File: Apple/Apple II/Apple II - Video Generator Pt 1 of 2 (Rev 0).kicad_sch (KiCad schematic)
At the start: 0 parts

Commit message: Finished Apple II - Sheet 14 - Video Generator Part 1 (Rev 0)
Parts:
- added A10: 74LS194, symbol Apple II:A10_74LS194
- added A3: 74166, symbol Apple II:A3_74166
- added A9: 74LS151, symbol Apple II:A9_74LS151
- added B10: 74LS74, symbol Apple II:B10_74LS74
- added B11: 74LS08, symbol Apple II:B11_74LS08
- added B12: 74LS11, symbol Apple II:B12_74LS11
- added B13: 74LS02, symbol Apple II:B13_74LS02
- added B2: 74S86, symbol Apple II:B2_74S86
- added B4: 74LS194, symbol Apple II:B4_74LS194
- added B9: 74LS194, symbol Apple II:B9_74LS194
- added C15: 0.1µF, symbol Device:C_Small
- added R12: 12K, symbol Device:R_US
- added R13: 3.3M, symbol Device:R_US
- added U?: A8_74LS257, symbol Apple II:A8_74LS257
- added U? (x2): B8_74LS174, symbol Apple II:B8_74LS174
- added U?: B5_74LS174, symbol Apple II:B5_74LS174
- added U?: B3_555, Package_SO:SOIC-8_3.9x4.9mm_P1.27mm, symbol Apple II:B3_555
- added U?: A5_2513, symbol Apple II:A5_2513
- added U?: B11_74LS08, symbol Apple II:B11_74LS08
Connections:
- new net: A10.4 (D1), U?.12 (ZD)
- new net: A9.15 (D4), B4.15 (Q0), U?.2 (0A)
- new net: A9.13 (D6), B9.15 (Q0), B9.7 (DSL), U?.3 (1A)
- new net: B4.7 (DSL), U?.4 (ZA)
- new net: A10.3 (D0), U?.7 (ZB)
- new net: B4.10 (S1), U?.9 (ZC)
- new net: A10.6 (D3), A3.2 (A), B13.4
- new net: B11.11, B13.5
- new net: A9.9 (C), U?.2 (Q0), U?.5
- new net: U?.15 (Q5), U?.3 (D0)
- new net: U?.14 (D4), U?.2 (Q0)
- new net: B13.13, U?.3 (D0)
- new net: R12.1, R13.2, U?.7 (DIS)
- new net: A10.12 (Q3), A3.1 (SER.IN), B2.12
- new net: A10.13 (Q2), A9.7 (~{ST})
- new net: A10.14 (Q1), A9.11 (A)
- new net: A10.15 (Q0), A9.10 (B)
- new net: B4.10 (S1), B9.10 (S1)
- new net: B4.11, B9.11
- new net: A9.14 (D5), B4.13 (Q2)
- new net: B4.9 (S0), B9.9 (S0)
- new net: A9.12 (D7), B9.13 (Q2)
- new net: C15.2, R13.1, U?.2 (TR), U?.6 (TH)
- new net: B11.13, U?.3 (OUT)
- new net: A9.1 (D3), A9.2 (D2), A9.3 (D1), A9.4 (D0), B2.11
- new net: A3.13 (Q_{H}), B2.13
- new net: A3.4 (C), U?.4 (D1)
- new net: A3.5 (D), U?.5 (D2)
- new net: A3.10 (E), U?.6 (D3)
- new net: A3.11 (F), U?.7 (D4)
- new net: A3.12 (G), U?.8 (D5)
- new net: B12.6, B13.11
- new net +5V: R12.2, U?.4 (~{R}), U?.8 (VCC)
- new net 14M: A10.11 (Cp), A3.7 (CL2), A9.5 (Y), B10.2 (D), B10.3 (CLK), B4.11, U?.1 (S), U?.4
- new net 7M_{36}: A3.6 (CL1)
- new net BLANKING: A10.5 (D2)
- new net DL0: B4.3 (D0), U?.17 (A4)
- new net DL1: B4.4 (D1), U?.18 (A5)
- new net DL2: B4.5 (D2), U?.19 (A6)
- new net DL3: B4.6 (D3), U?.20 (A7)
- new net DL4: B9.3 (D0), U?.21 (A8)
- new net DL5: B9.4 (D1), U?.22 (A9)
- new net DL6: B11.12, B9.5 (D2)
- new net DL7: B13.6, B9.6 (D3)
- new net Earth: A3.14 (H), A3.3 (B), C15.1, U?.1 (GND), U?.10 (GND), U?.11 (~{CE}), U?.13 (1D), U?.15 (~{E}), U?.6 (1B)
- new net H0: U?.14 (0D)
- new net HIRES: U?.6
- new net LD194: A10.10 (S1), A10.9 (S0), B4.9 (S0)
- new net MIX MODE: B12.5
- new net SOFT 5: A3.9 (~{CLR}), B10.1 (~{CLR}), B10.4 (~{P}), U?.1 (~{CLR}), U?.1 (~{CLR}), U?.1 (~{CLR}), U?.11 (0C)
- new net TEXT MODE: B13.12
- new net V2: B12.3
- new net V4: B12.4
- new net VA: U?.14 (A1)
- new net VB: U?.15 (A2)
- new net VC: U?.16 (A3), U?.5 (0B)
- new net VIDEO_DATA: B10.5 (Q)
- new net ~{7M}: U?.10 (1C)
- new net ~{LDPS}: A3.15 (~{LD})
- new net ~{RAS}: U?.9 (Cp), U?.9 (Cp), U?.9 (Cp)
- no-connect marks 0 -> 1
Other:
- note added: "FROM CLOCK GENERATOR"
- note added: "FROM ON-BOARD I/O"
- note added: "FROM PART 2"
- note added: "FROM RAM"
- note added: "FROM VIDEO ADDRESS GENERATOR"
- note added: "TO MEMORY ADDRESS"
- note added: "TO PART 2"
- title: (none) -> Apple II - Video Generator Part 1

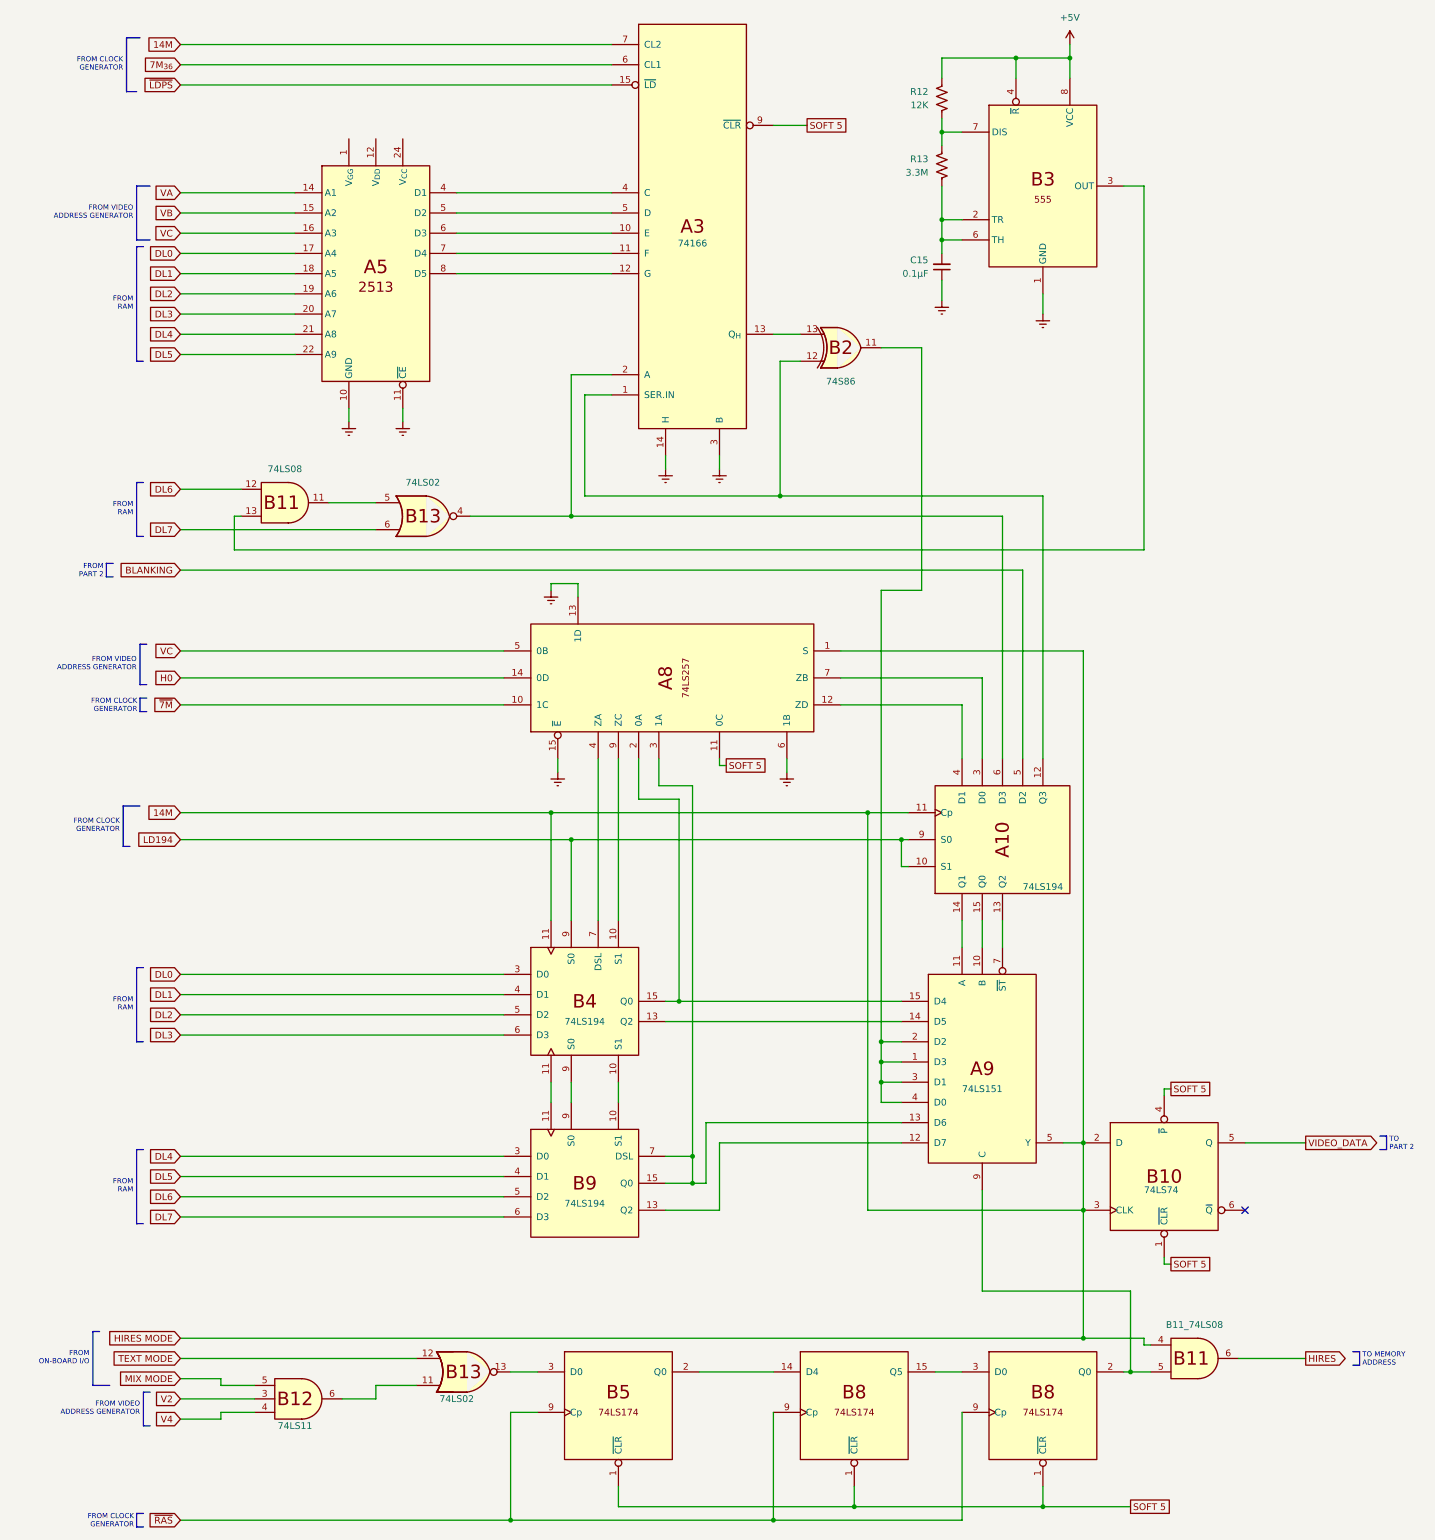
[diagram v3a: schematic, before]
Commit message: Finished Apple II - Sheet 15 - Video Generator Part 1 (Rev 1)
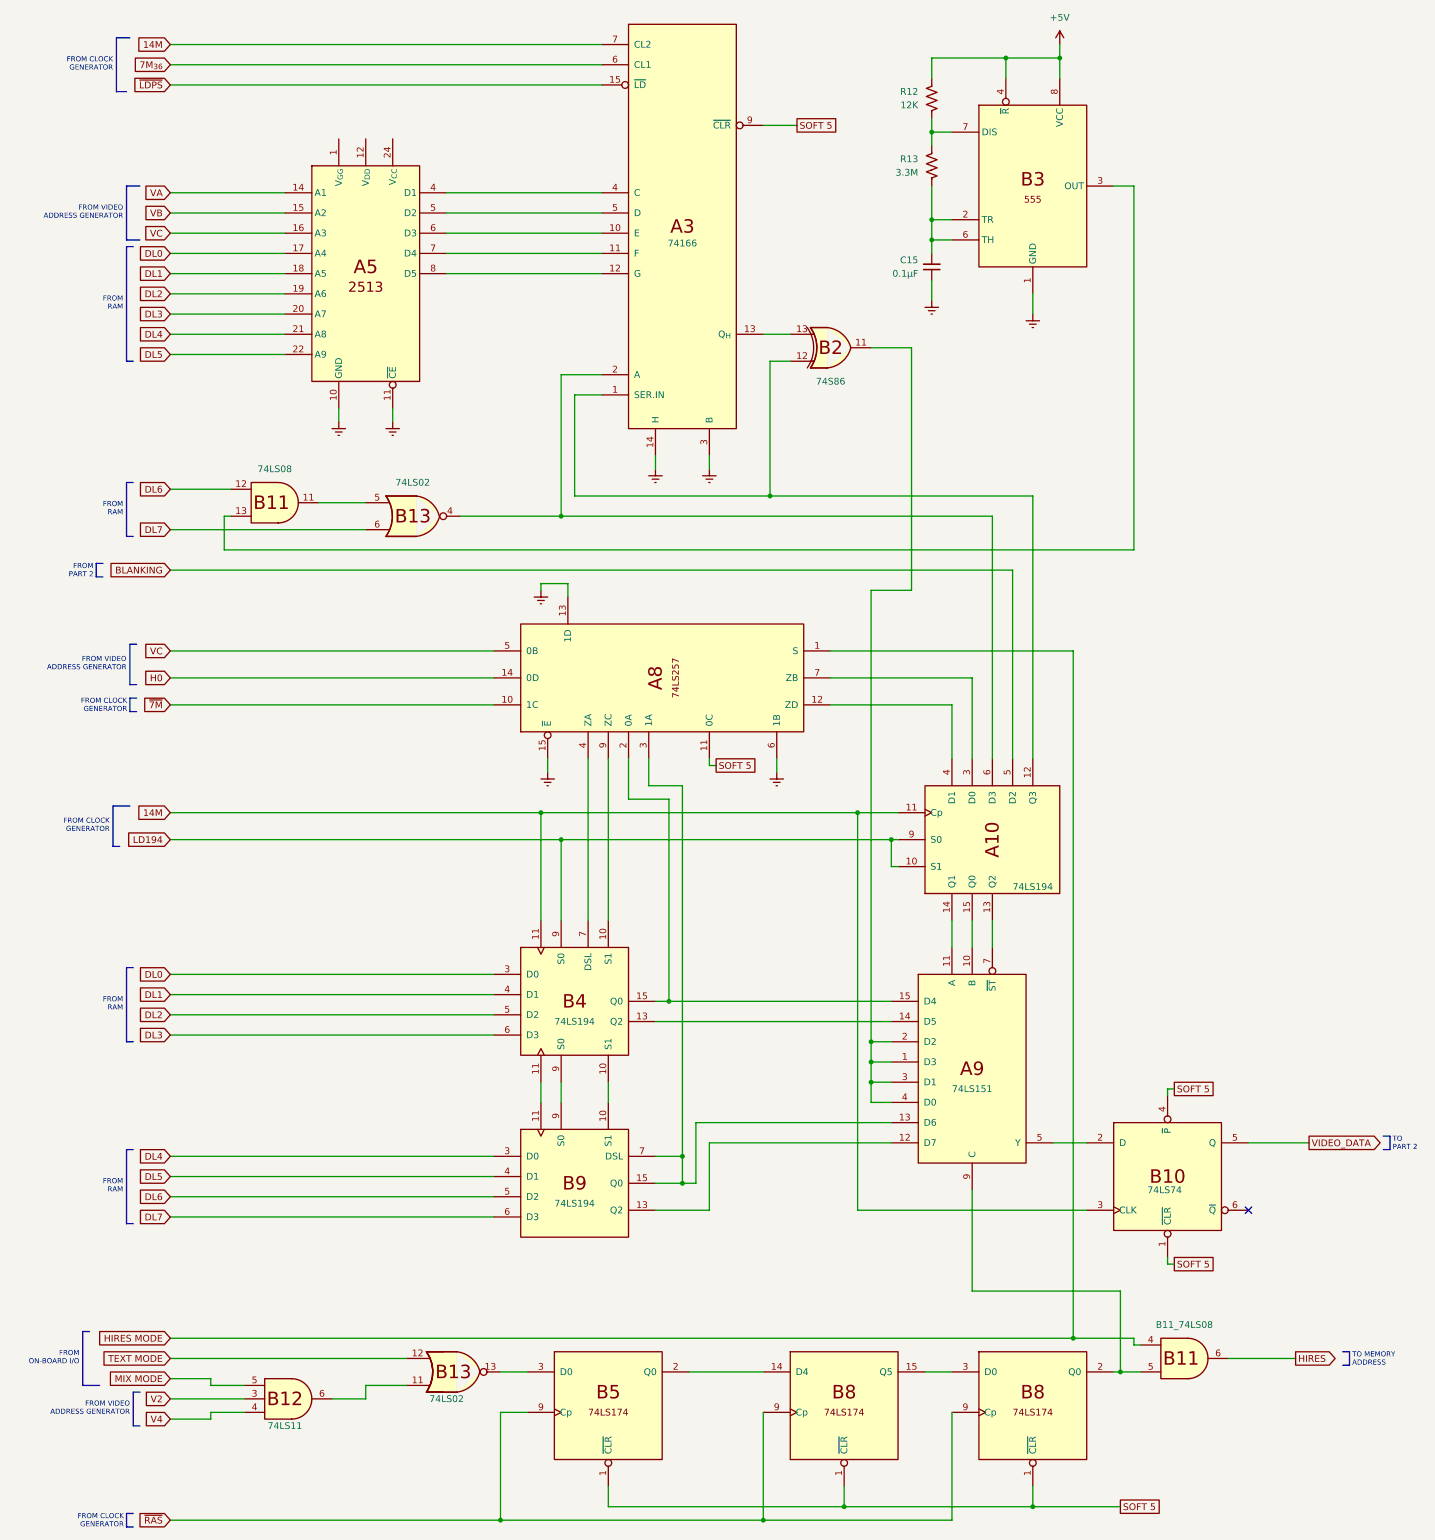
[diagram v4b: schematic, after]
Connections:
- net 14M: no longer A9.5 (Y), B10.2 (D), U?.1 (S), U?.4
- new net: A9.5 (Y), B10.2 (D)
- new net HIRES MODE: U?.1 (S), U?.4
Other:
- moved on the sheet: C15, R12, R13

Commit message: Finished Apple II - Sheet 16 - Video Generator Part 1 (Rev 7, RFI)
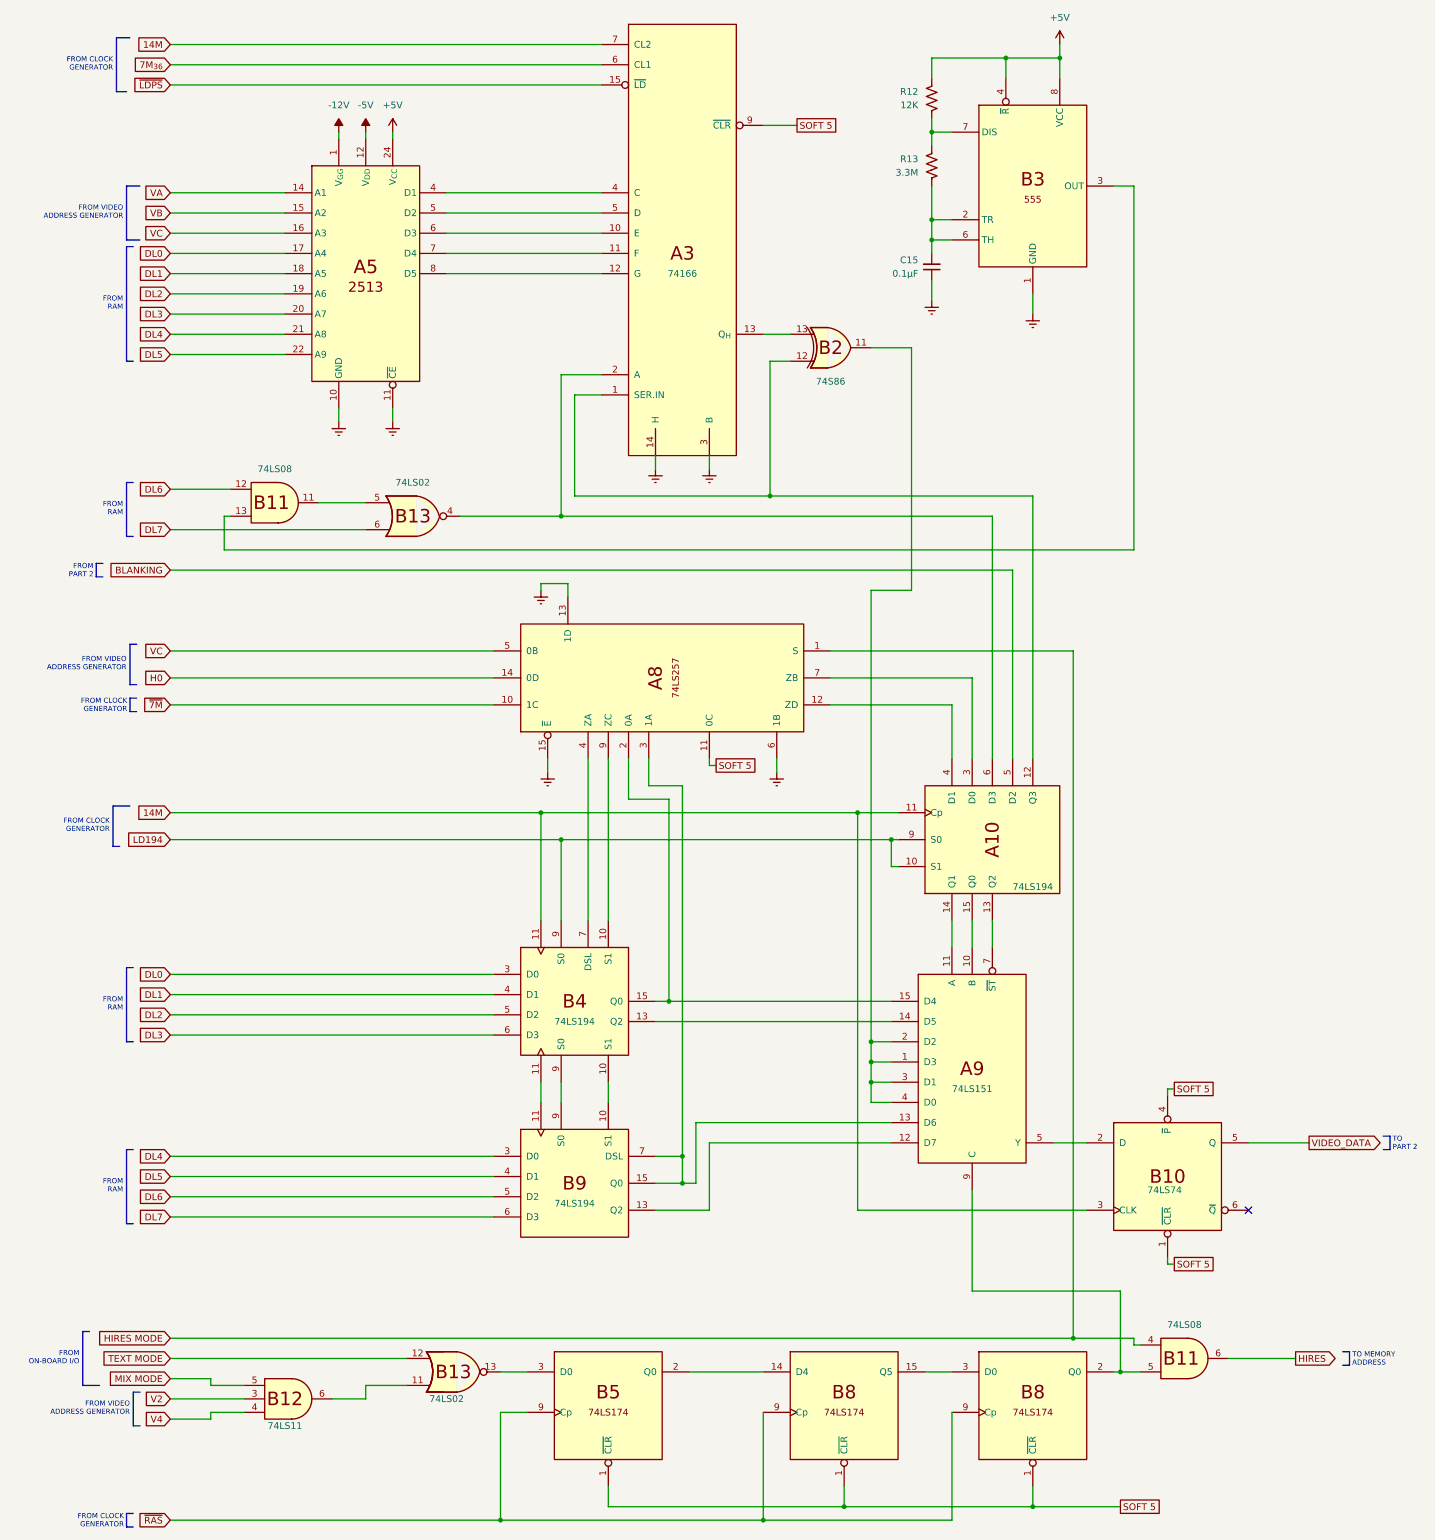
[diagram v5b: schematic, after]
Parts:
- B11: renamed from U?; value B11_74LS08 -> 74LS08
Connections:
- net +5V: now also U?.24 (V_{CC})
- net -12V: now reaches U?.1 (V_{GG})
- net -5V: now reaches U?.12 (V_{DD})
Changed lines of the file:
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@@
+    (stroke (width 0) (type default) (color 0 0 0 0))
+  )
+  (wire (pts (xy 82.55 76.2) (xy 82.55 77.47))
     (stroke (width 0) (type default) (color 0 0 0 0))
   )
@@
     (stroke (width 0) (type default) (color 0 0 0 0))
   )
+  (wire (pts (xy 87.63 76.2) (xy 87.63 77.47))
+    (stroke (width 0) (type default) (color 0 0 0 0))
+  )
   (polyline (pts (xy 38.735 281.94) (xy 37.465 281.94))
     (stroke (width 0) (type solid) (color 0 0 0 0))
@@
   )
   (wire (pts (xy 162.56 114.3) (xy 157.48 114.3))
+    (stroke (width 0) (type default) (color 0 0 0 0))
+  )
+  (wire (pts (xy 77.47 76.2) (xy 77.47 77.47))
     (stroke (width 0) (type default) (color 0 0 0 0))
   )
@@
     )
     (property "Datasheet" "~" (id 3) (at 147.32 139.7 0)
+      (effects (font (size 1.27 1.27)) hide)
+    )
+    (pin "1")
+  )
+  (symbol (lib_id "power:-12V") (at 77.47 76.2 0) (unit 1)
+    (in_bom yes) (on_board yes) (fields_autoplaced)
+    (property "Reference" "#PWR?" (id 0) (at 77.47 73.66 0)
+      (effects (font (size 1.27 1.27)) hide)
+    )
+    (property "Value" "-12V" (id 1) (at 77.47 71.12 0))
+    (property "Footprint" "" (id 2) (at 77.47 76.2 0)
+      (effects (font (size 1.27 1.27)) hide)
+    )
+    (property "Datasheet" "" (id 3) (at 77.47 76.2 0)
       (effects (font (size 1.27 1.27)) hide)
     )
@@
     (pin "8")
   )
+  (symbol (lib_id "power:-5V") (at 82.55 76.2 0) (unit 1)
+    (in_bom yes) (on_board yes) (fields_autoplaced)
+    (property "Reference" "#PWR?" (id 0) (at 82.55 73.66 0)
+      (effects (font (size 1.27 1.27)) hide)
+    )
+    (property "Value" "-5V" (id 1) (at 82.55 71.12 0))
+    (property "Footprint" "" (id 2) (at 82.55 76.2 0)
+      (effects (font (size 1.27 1.27)) hide)
+    )
+    (property "Datasheet" "" (id 3) (at 82.55 76.2 0)
+      (effects (font (size 1.27 1.27)) hide)
+    )
+    (pin "1")
+  )
+  (symbol (lib_id "power:+5V") (at 87.63 76.2 0) (unit 1)
+    (in_bom yes) (on_board yes) (fields_autoplaced)
+    (property "Reference" "#PWR?" (id 0) (at 87.63 80.01 0)
+      (effects (font (size 1.27 1.27)) hide)
+    )
+    (property "Value" "+5V" (id 1) (at 87.63 71.12 0))
+    (property "Footprint" "" (id 2) (at 87.63 76.2 0)
+      (effects (font (size 1.27 1.27)) hide)
+    )
+    (property "Datasheet" "" (id 3) (at 87.63 76.2 0)
+      (effects (font (size 1.27 1.27)) hide)
+    )
+    (pin "1")
+  )
   (symbol (lib_id "Device:C_Small") (at 189.23 101.6 0) (mirror x) (unit 1)
     (in_bom yes) (on_board yes) (fields_autoplaced)
@@
       (effects (font (size 1.27 1.27)) hide)
     )
-    (property "Value" "74166" (id 1) (at 142.24 97.155 0))
+    (property "Value" "74166" (id 1) (at 142.24 102.87 0))
     (property "Footprint" "" (id 2) (at 132.08 55.88 0)
       (effects (font (size 1.27 1.27)) hide)
@@
   (symbol (lib_id "Apple II:B11_74LS08") (at 236.22 307.34 0) (unit 2)
     (in_bom yes) (on_board yes) (fields_autoplaced)
-    (property "Reference" "U?" (id 0) (at 204.47 285.75 0)
-      (effects (font (size 1.27 1.27)) hide)
-    )
-    (property "Value" "B11_74LS08" (id 1) (at 236.855 300.99 0))
+    (property "Reference" "B11" (id 0) (at 204.47 285.75 0)
+      (effects (font (size 1.27 1.27)) hide)
+    )
+    (property "Value" "74LS08" (id 1) (at 236.855 300.99 0))
     (property "Footprint" "" (id 2) (at 237.49 307.34 0)
       (effects (font (size 1.27 1.27)) hide)
